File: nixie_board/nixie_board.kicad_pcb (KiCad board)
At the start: 2 copper layers, 227.3 x 61 mm, 87 parts, among them J1 12V, J2 170V, J3 GND, J4 SHDN, J5 Barrel_Jack_Switch, M1 MountingHole_3.2mm_M3, M2 MountingHole_3.2mm_M3, M3 MountingHole_3.2mm_M3, M4 MountingHole_3.2mm_M3, Q1 MPSA42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

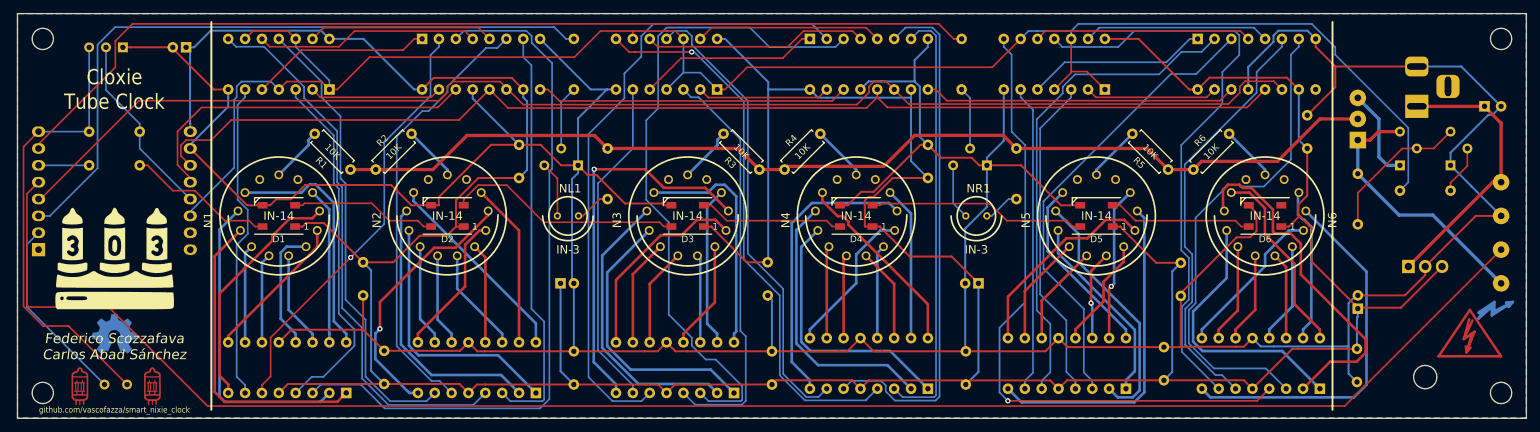
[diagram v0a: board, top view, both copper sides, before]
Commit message: massive update + migration to platformIO +  v2 HW preparation
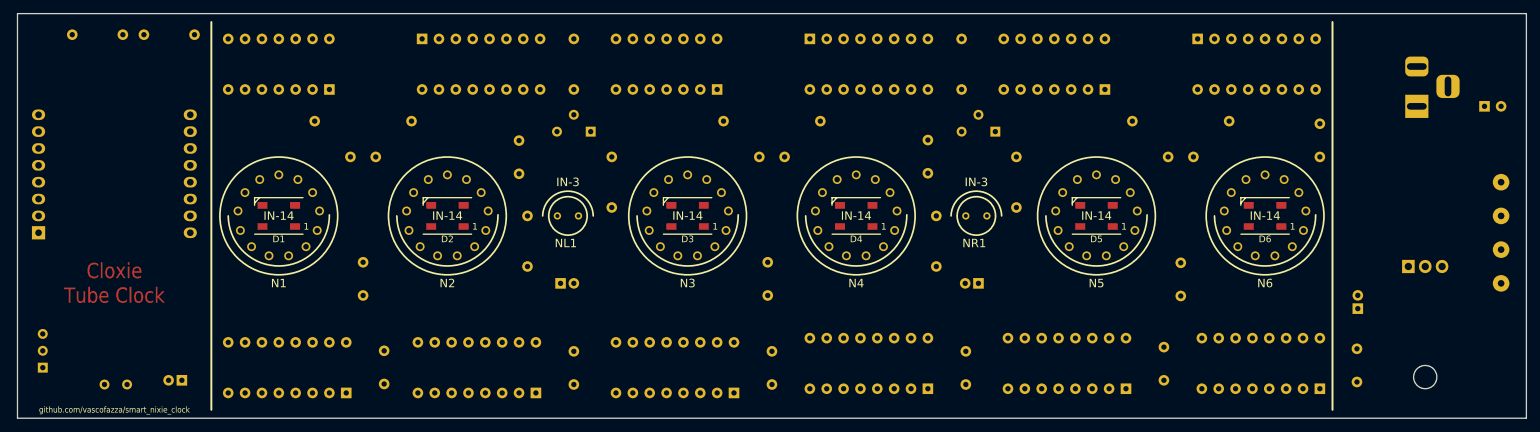
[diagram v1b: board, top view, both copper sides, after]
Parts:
- removed JP1: Jumper_3_Bridged12, Connector_Wire:SolderWirePad_1x03_P3.175mm_Drill1mm
- removed M1, M2, M3, M4: MountingHole_3.2mm_M3, MountingHole:MountingHole_3.2mm_M3
- removed Q3, Q4: MPSA42, Package_TO_SOT_THT:TO-92_Wide
- removed S1: Symbol_Highvoltage_Type1_CopperTop_Small, Symbol:Symbol_Highvoltage_Type1_CopperTop_Small
- removed S10, S11, S12, S7, S8, S9: LOGO, Symbol:tube_silk
- removed S13, S6: LOGO, Symbol:tube
- removed S14: LOGO, Symbol:nixie_clock
- removed S2: Symbol_HighVoltage_Type2_CopperTop_VerySmall, Symbol:Symbol_HighVoltage_Type2_CopperTop_VerySmall
- removed S3: OSHW-Symbol_6.7x6mm_Copper, Symbol:OSHW-Symbol_6.7x6mm_Copper
- R1, R2, R3, R4, R5, R6: moved to B.Cu
- R10, R12, R14: value 10K -> 150K
- R15: value 100K -> 150K
- U11, U14, U2, U5, U7, U9: value K155NA1 -> K155ID1
- moved Q1 129.6 mm to (127.0, 39.4), turned to 180 degrees
- moved R10 118.9 mm to (130.2, 43.2), turned to 270 degrees
- moved R15 63.8 mm to (179.1, 52.1)
- moved Q2 63.1 mm to (188.0, 39.4)
- moved C16 50.2 mm to (65.4, 76.8)
- moved U15 49.7 mm to (44.5, 74.9), turned to 90 degrees
- moved R8 21.3 mm to (59.7, 24.8)
- moved R12 15.8 mm to (117.5, 52.1)
- moved R9 14.8 mm to (48.9, 24.8)
- moved U3 2.54 mm to (43.8, 54.6)
- moved C14 2.29 mm to (236.9, 43.2)
- moved R1 1.91 mm to (90.8, 43.2)
- moved R2 1.91 mm to (94.6, 43.2)
- moved R3 1.91 mm to (152.4, 43.2)
- moved R4 1.91 mm to (156.2, 43.2)
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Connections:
- D6 pad 2: Net-(D6-Pad2) -> (no net)
- J5 pad 3: Net-(J5-Pad3) -> (no net)
- N1 pad LHDP: Net-(N1-PadLHDP) -> (no net)
- N1 pad RHDP: Net-(N1-PadRHDP) -> (no net)
- N2 pad LHDP: Net-(N2-PadLHDP) -> (no net)
- N2 pad RHDP: Net-(N2-PadRHDP) -> (no net)
- N3 pad LHDP: Net-(N3-PadLHDP) -> (no net)
- N3 pad RHDP: Net-(N3-PadRHDP) -> (no net)
- N4 pad LHDP: Net-(N4-PadLHDP) -> (no net)
- N4 pad RHDP: Net-(N4-PadRHDP) -> (no net)
- N5 pad LHDP: Net-(N5-PadLHDP) -> (no net)
- N5 pad RHDP: Net-(N5-PadRHDP) -> (no net)
- N6 pad LHDP: Net-(N6-PadLHDP) -> (no net)
- N6 pad RHDP: Net-(N6-PadRHDP) -> (no net)
- Q1 pad 3: Net-(Q1-Pad3) -> Net-(NL1-PadK)
- Q2 pad 3: Net-(NL1-PadK) -> Net-(NR1-PadK)
- R1 pad 1: Net-(JP1-Pad2) -> /170V
- R10 pad 1: /STROBE -> /170V
- R10 pad 2: Net-(Q1-Pad2) -> Net-(NL1-PadA)
- R11 pad 1: Net-(Q2-Pad2) -> Net-(Q1-Pad2)
- R12 pad 1: Net-(JP1-Pad2) -> Net-(NL1-PadA)
- R12 pad 2: Net-(NL1-PadA) -> GND
- R13 pad 1: Net-(Q3-Pad2) -> Net-(Q2-Pad2)
- R14 pad 1: Net-(JP1-Pad2) -> /170V
- R15 pad 1: /170V -> Net-(NR1-PadA)
- R15 pad 2: Net-(Q1-Pad3) -> GND
- R2 pad 1: Net-(JP1-Pad2) -> /170V
- R3 pad 1: Net-(JP1-Pad2) -> /170V
- R4 pad 1: Net-(JP1-Pad2) -> /170V
- R5 pad 1: Net-(JP1-Pad2) -> /170V
- R6 pad 1: Net-(JP1-Pad2) -> /170V
- U13 pad 9: Net-(U13-Pad9) -> (no net)
- U3 pad 1: Net-(U3-Pad1) -> (no net)
- U3 pad 15: Net-(U3-Pad15) -> (no net)
- U3 pad 16: Net-(U3-Pad16) -> (no net)
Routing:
- net GND: track 630.9 -> 0.00 mm
- net /5V: track 600.8 -> 0.00 mm
- net /STROBE: track 271.4 -> 0.00 mm
- net /SHUTDOWN: track 257.4 -> 0.00 mm
- net /SRCLK: track 202.7 -> 0.00 mm
- net /RCLK: track 175.2 -> 0.00 mm
- net Net-(JP1-Pad2): track 163.4 -> 0.00 mm
- net /RIGHT_DOT: track 151.1 -> 0.00 mm
- net Net-(U2-Pad3): track 106.6 -> 0.00 mm
- net /LEFT_DOT: track 104.1 -> 0.00 mm
- net Net-(U7-Pad3): track 99.5 -> 0.00 mm
- net Net-(U10-Pad8): track 98.1 -> 0.00 mm, vias 1 -> 0
- net Net-(U7-Pad6): track 95.5 -> 0.00 mm
- net Net-(U10-Pad11): track 89.7 -> 0.00 mm
- net Net-(U6-Pad8): track 83.6 -> 0.00 mm, vias 1 -> 0
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- removed copper zone on B.Cu, net GND
- removed copper zone on F.Cu, net GND
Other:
- board text removed: "D"
- board text removed: "Federico Scozzafava Carlos Abad Sánchez"
- board text removed: "Q"

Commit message: pcb REV1
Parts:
- removed U12: L7805, Package_TO_SOT_THT:TO-220-3_Horizontal_TabDown
- added J6: 5V, Connector_Wire:SolderWirePad_1x01_Drill1mm, B.Cu at (254.0, 59.7)
- added M1: MountingHole_3.2mm_M3_Pad_Via, MountingHole:MountingHole_3.2mm_M3_Pad_Via, F.Cu at (254.0, 30.5)
- added M11: MountingHole_2mm, MountingHole:MountingHole_2mm, F.Cu at (203.2, 52.1)
- added M12: MountingHole_2mm, MountingHole:MountingHole_2mm, F.Cu at (228.6, 52.1)
- added M2: MountingHole_3.2mm_M3_Pad_Via, MountingHole:MountingHole_3.2mm_M3_Pad_Via, F.Cu at (254.0, 73.7)
- added M3: MountingHole_3.2mm_M3_Pad_Via, MountingHole:MountingHole_3.2mm_M3_Pad_Via, F.Cu at (54.6, 73.7)
- added M4: MountingHole_3.2mm_M3_Pad_Via, MountingHole:MountingHole_3.2mm_M3_Pad_Via, F.Cu at (54.6, 30.5)
- added M5: MountingHole_2mm, MountingHole:MountingHole_2mm, F.Cu at (80.0, 52.1)
- added M6: MountingHole_2mm, MountingHole:MountingHole_2mm, F.Cu at (105.4, 52.1)
- added M8: MountingHole_2mm, MountingHole:MountingHole_2mm, F.Cu at (141.6, 52.1)
- added M9: MountingHole_2mm, MountingHole:MountingHole_2mm, F.Cu at (167.0, 52.1)
- added R16: 10K, Resistor_THT:R_Axial_DIN0207_L6.3mm_D2.5mm_P7.62mm_Horizontal, B.Cu at (67.3, 74.9)
- added S0: Symbol_HighVoltage_Type2_CopperTop_VerySmall, Symbol:Symbol_HighVoltage_Type2_CopperTop_VerySmall, F.Cu at (245.1, 55.2)
- added S1: Symbol_Barrel_Polarity, Symbol:Symbol_Barrel_Polarity, B.Cu at (252.1, 38.1)
- added S10: LOGO, Symbol:tube_silk, B.Cu at (154.3, 52.1)
- added S11: LOGO, Symbol:tube_silk, B.Cu at (215.9, 52.1)
- added S12: LOGO, Symbol:tube_silk, F.Cu at (54.6, 36.8)
- added S13: LOGO, Symbol:tube_silk, F.Cu at (54.6, 67.9)
- added S2, S2b: OSHW-Symbol_6.7x6mm_Copper, Symbol:OSHW-Symbol_6.7x6mm_Copper, B.Cu at (55.2, 52.7)
- added S4: LOGO, Symbol:tube, F.Cu at (54.6, 36.8)
- added S5: LOGO, Symbol:tube, F.Cu at (54.6, 67.9)
- added S6: LOGO, Symbol:tube_silk, F.Cu at (154.3, 52.1)
- added S7: LOGO, Symbol:tube_silk, F.Cu at (92.7, 52.1)
- added S8: LOGO, Symbol:tube_silk, F.Cu at (215.9, 52.1)
- added S9: LOGO, Symbol:tube_silk, B.Cu at (92.7, 52.1)
- R10, R14: value 150K -> 130K
- moved U15 44.9 mm to (63.5, 34.3), turned to 180 degrees
- moved R9 22.7 mm to (67.3, 38.1), turned to 90 degrees
- moved R8 21.3 mm to (67.9, 44.5), turned to 270 degrees
- moved U3 20.7 mm to (59.7, 41.3), turned to 270 degrees
- moved C7 20.7 mm to (246.4, 49.5), turned to 180 degrees
- moved J2 20.5 mm to (254.0, 44.5)
- moved C16 19.7 mm to (64.8, 57.1)
- moved J4 12.7 mm to (254.0, 64.8)
- moved J1 10.5 mm to (254.0, 49.5)
- moved J3 10.5 mm to (254.0, 54.6)
- moved R7 9.16 mm to (62.2, 69.8), turned to 270 degrees
- moved J5 9.12 mm to (244.2, 41.1)
- moved C17 7.41 mm to (246.4, 59.7), turned to 180 degrees
- moved U4 6.75 mm to (97.2, 30.5)
- moved U10 6.35 mm to (208.3, 38.1)
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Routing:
- net GND: track 0.00 -> 594.7 mm
- net /5V: track 0.00 -> 552.4 mm, vias 0 -> 2
- net /STROBE: track 0.00 -> 222.4 mm
- net /SHUTDOWN: track 0.00 -> 215.9 mm
- net /RCLK: track 0.00 -> 180.9 mm, vias 0 -> 1
- net /170V: track 0.00 -> 179.2 mm, vias 0 -> 1
- net /SRCLK: track 0.00 -> 176.3 mm
- net /RIGHT_DOT: track 0.00 -> 116.3 mm
- net Net-(U6-Pad8): track 0.00 -> 94.2 mm
- net Net-(U10-Pad8): track 0.00 -> 89.5 mm
- net /SER: track 0.00 -> 76.0 mm
- net Net-(U7-Pad6): track 0.00 -> 70.8 mm
- net Net-(U1-Pad8): track 0.00 -> 70.2 mm, vias 0 -> 1
- net Net-(U4-Pad6): track 0.00 -> 65.7 mm
- net /LEFT_DOT: track 0.00 -> 64.8 mm
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- added copper zone on B.Cu, net GND
- added copper zone on F.Cu, net GND
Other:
- board size 227.3 x 61 mm -> 207 x 50.8 mm
- net class HighVoltageIN: clearance 0.35 -> 0.3; trace_width 0.5 -> 0.35
- net class HighVoltageOut: trace_width 0.4 -> 0.35
- board text added: "+"
- board text added: "-"
- board text added: "12V DC"
- board text added: "Federico Scozzafava 2020"
- board text added: "REV1"

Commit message: board rev2
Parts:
- removed J2: 170V, Connector_Wire:SolderWirePad_1x01_Drill1mm
- removed J3: GND, Connector_Wire:SolderWirePad_1x01_Drill1mm
- removed J4: SHDN, Connector_Wire:SolderWirePad_1x01_Drill1mm
- removed J6: 5V, Connector_Wire:SolderWirePad_1x01_Drill1mm
- removed M1, M2, M3, M4: MountingHole_3.2mm_M3_Pad_Via, MountingHole:MountingHole_3.2mm_M3_Pad_Via
- removed M11, M12, M5, M6, M8, M9: MountingHole_2mm, MountingHole:MountingHole_2mm
- removed S0: Symbol_HighVoltage_Type2_CopperTop_VerySmall, Symbol:Symbol_HighVoltage_Type2_CopperTop_VerySmall
- added H1: MountingHole_Pad, MountingHole:MountingHole_3.2mm_M3_Pad_Via, F.Cu at (250.2, 30.5)
- added H2: MountingHole_Pad, MountingHole:MountingHole_3.2mm_M3_Pad_Via, F.Cu at (58.4, 30.5)
- added H3: MountingHole_Pad, MountingHole:MountingHole_3.2mm_M3_Pad_Via, F.Cu at (250.2, 73.7)
- added H4: MountingHole_Pad, MountingHole:MountingHole_3.2mm_M3_Pad_Via, F.Cu at (58.4, 73.7)
- added S15: LOGO, Symbol:tube_silk, B.Cu at (228.6, 52.1)
- added S16: LOGO, Symbol:tube_silk, B.Cu at (167.0, 52.1)
- added S17: LOGO, Symbol:tube_silk, B.Cu at (105.4, 52.1)
- J1: value 12V -> POWER; footprint Connector_Wire:SolderWirePad_1x01_Drill1mm -> TerminalBlock:TerminalBlock_bornier-5_P5.08mm; moved to F.Cu
- moved R16 16.8 mm to (64.1, 58.4), turned to 0 degrees
- moved C4 16.7 mm to (156.8, 57.1), turned to 270 degrees
- moved C2 16.7 mm to (218.4, 57.1), turned to 270 degrees
- moved C6 16.4 mm to (95.2, 57.1), turned to 270 degrees
- moved C16 16.2 mm to (73.0, 71.1)
- moved S10 12.7 mm to (141.6, 52.1)
- moved S11 12.7 mm to (203.2, 52.1)
- moved S9 12.7 mm to (80.0, 52.1)
- moved C14 11.9 mm to (233.7, 35.5)
- moved U13 7.73 mm to (210.8, 29.2)
- moved R9 7.10 mm to (64.1, 44.5), turned to 270 degrees
- moved C1 6.99 mm to (240.7, 68.6), turned to 0 degrees
- moved U2 6.35 mm to (96.5, 74.9)
- moved U15 5.85 mm to (69.2, 33.0)
- moved J1 5.85 mm to (249.6, 45.7)
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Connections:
- J1 pad 1: Net-(C7-Pad1) -> /170V
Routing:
- net GND: track 594.7 -> 712.0 mm
- net /SER: track 76.0 -> 50.6 mm
- net Net-(C7-Pad1): track 16.9 -> 42.0 mm
- net Net-(N6-Pad9): track 38.4 -> 61.5 mm
- net Net-(N1-Pad9): track 40.2 -> 63.2 mm, vias 0 -> 1
- net Net-(N1-Pad3): track 35.8 -> 16.3 mm
- net Net-(U4-Pad6): track 65.7 -> 82.8 mm
- net Net-(U2-Pad3): track 52.5 -> 67.1 mm, vias 0 -> 1
- net /STROBE: track 222.4 -> 208.0 mm
- net /SRCLK: track 176.3 -> 161.9 mm
- net /SHUTDOWN: track 215.9 -> 201.6 mm
- net Net-(N6-Pad3): track 20.6 -> 34.3 mm
- net Net-(U11-Pad3): track 62.9 -> 76.2 mm, vias 0 -> 1
- net Net-(U11-Pad6): track 61.8 -> 74.6 mm
- net Net-(N1-Pad8): track 47.9 -> 60.4 mm
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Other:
- board size 207 x 50.8 mm -> 199.4 x 50.8 mm
- net class 5v rail: trace_width 0.3 -> 0.35
- net class Default: clearance 0.254 -> 0.2; trace_width 0.254 -> 0.2; via_dia 0.8 -> 0.6
- net class HighVoltageIN: clearance 0.3 -> 0.508; trace_width 0.35 -> 0.55
- net class HighVoltageOut: clearance 0.3 -> 0.508; trace_width 0.35 -> 0.254
- rule trace_clearance: 0.254 -> 0.2
- board text added: "5V"
- board text added: "GND"
- board text added: "HIGH VOLTAGE"
- board text added: "HV"
- board text added: "REV2"
- board text added: "SHDN"
- board text added: "VIN"
- board text removed: "REV1"

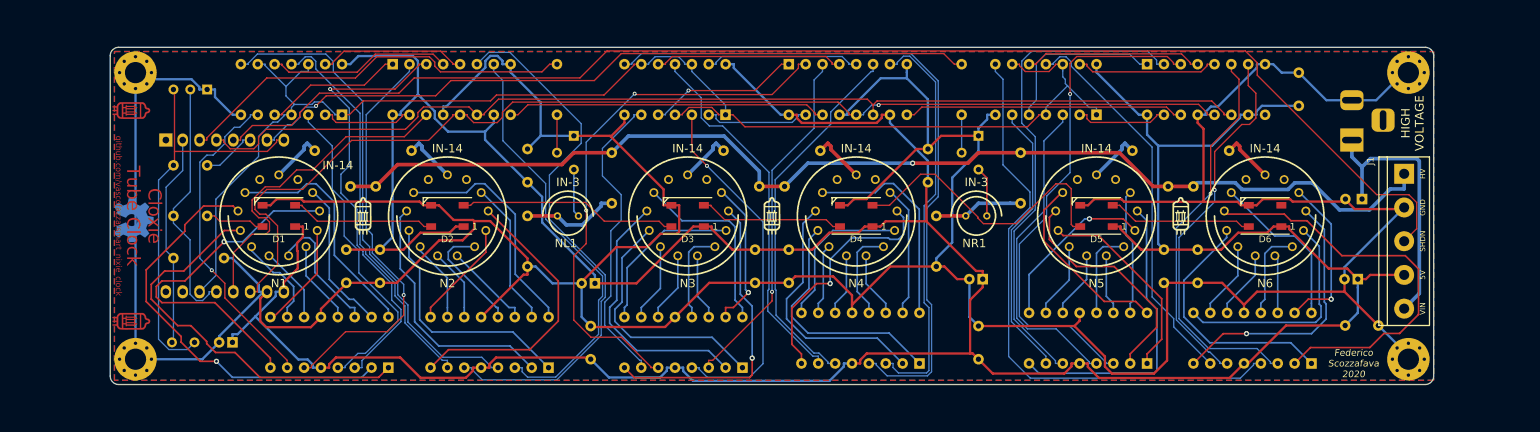
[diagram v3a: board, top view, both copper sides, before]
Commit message: rev2 board fix
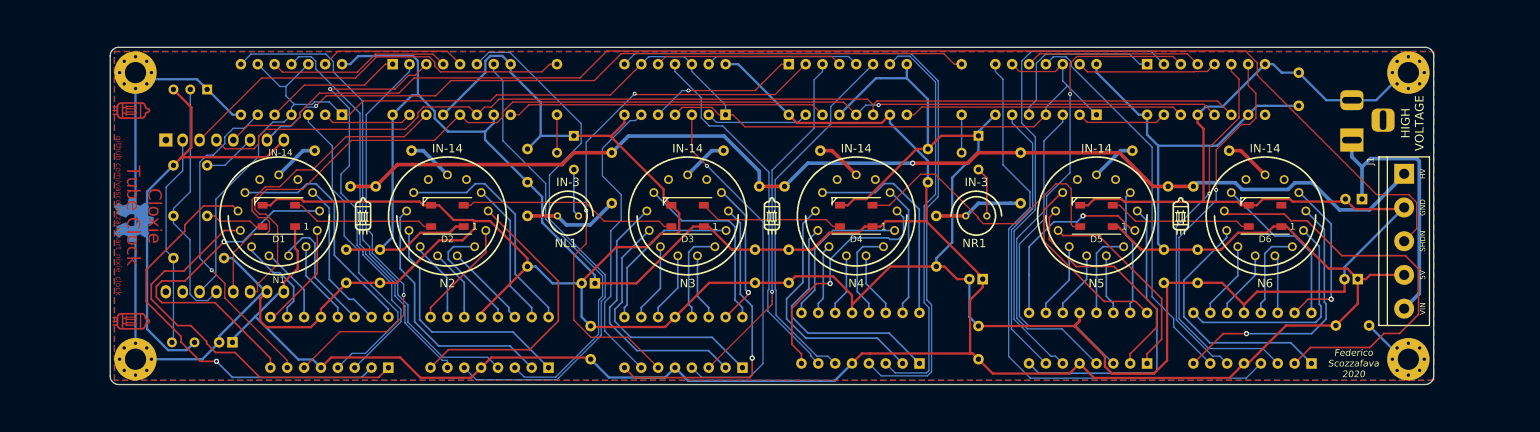
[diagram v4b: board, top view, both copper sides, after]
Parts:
- moved C1 1.40 mm to (239.3, 68.6)
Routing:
- net /5V: track 562.6 -> 553.7 mm
- net GND: track 712.0 -> 706.6 mm
- net /3.3V: track 62.6 -> 65.6 mm
- net Net-(N5-Pad3): track 25.9 -> 28.7 mm
- net /STROBE: track 208.0 -> 205.7 mm
- net /RIGHT_DOT: track 111.3 -> 113.2 mm
- net /170V: track 176.9 -> 175.7 mm
- net Net-(N6-PadA): track 8.12 -> 6.92 mm
- net Net-(N4-PadA): track 8.12 -> 6.92 mm
- net Net-(N2-PadA): track 8.12 -> 6.92 mm
- net Net-(N5-PadA): track 8.12 -> 6.92 mm
- net Net-(N3-PadA): track 8.12 -> 6.92 mm
- net Net-(N1-PadA): track 8.12 -> 6.92 mm
- net /RCLK: track 172.9 -> 172.2 mm
- net Net-(U2-Pad3): track 67.1 -> 66.4 mm
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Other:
- board text added: "11/20"
- board text added: "D"
